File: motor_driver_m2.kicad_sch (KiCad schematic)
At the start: 32 parts, among them J7 Conn_01x01_Pin, J8 Conn_01x01_Pin, J9 Conn_01x01_Pin, M2 DRV8320SRTVR, Q10 NP80N06D6, Q11 NP80N06D6, Q12 NP80N06D6, Q7 NP80N06D6, Q8 NP80N06D6, Q9 NP80N06D6

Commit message: ...
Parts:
- C28: renamed from C25; footprint easyeda2kicad:C0603 -> easyeda2kicad:C0402
- renumbered C24 to C27, C26 to C29, C27 to C30, C28 to C31, C29 to C32, C30 to C33, C31 to C34, J8 to J7, J9 to J8, J7 to J9, R23 to R21, R27 to R22, R28 to R23, R29 to R24, R30 to R25, R31 to R26, R32 to R27, R33 to R28, R34 to R29, R35 to R30, R36 to R31, R37 to R32, R38 to R33, R39 to R34
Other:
- moved on the sheet: J7, J8, J9

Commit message: ...
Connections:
- net SCLK: no longer names the net of M2.20 (SCLK)
- net SDI: no longer names the net of M2.19 (SDI)
- net SDO: no longer names the net of M2.18 (SDO)
- no-connect marks 0 -> 3
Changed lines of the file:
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@@
 		(color 0 0 0 0)
 	)
+	(no_connect
+		(at 92.71 80.01)
+	)
+	(no_connect
+		(at 92.71 77.47)
+	)
+	(no_connect
+		(at 92.71 74.93)
+	)
 	(wire
 		(pts
@@
 	(wire
 		(pts
-			(xy 105.41 74.93) (xy 92.71 74.93)
-		)
-		(stroke
-			(width 0)
-			(type default)
-		)
-	)
-	(wire
-		(pts
 			(xy 105.41 57.15) (xy 92.71 57.15)
 		)
@@
 	(wire
 		(pts
-			(xy 105.41 77.47) (xy 92.71 77.47)
-		)
-		(stroke
-			(width 0)
-			(type default)
-		)
-	)
-	(wire
-		(pts
 			(xy 77.47 161.29) (xy 77.47 162.56)
 		)
@@
 	(wire
 		(pts
-			(xy 92.71 80.01) (xy 105.41 80.01)
-		)
-		(stroke
-			(width 0)
-			(type default)
-		)
-	)
-	(wire
-		(pts
 			(xy 21.59 50.8) (xy 21.59 49.53)
 		)
@@
 		)
 	)
-	(global_label "SCLK"
-		(shape input)
-		(at 105.41 74.93 0)
-		(fields_autoplaced yes)
-		(effects
-			(font
-				(size 1.27 1.27)
-			)
-			(justify left)
-		)
-		(property "Intersheetrefs" "${INTERSHEET_REFS}"
-			(at 113.1728 74.93 0)
-			(effects
-				(font
-					(size 1.27 1.27)
-				)
-				(justify left)
-				(hide yes)
-			)
-		)
-	)
 	(global_label "B+"
 		(shape input)
@@
 		)
 	)
-	(global_label "SDO"
-		(shape input)
-		(at 105.41 80.01 0)
-		(fields_autoplaced yes)
-		(effects
-			(font
-				(size 1.27 1.27)
-			)
-			(justify left)
-		)
-		(property "Intersheetrefs" "${INTERSHEET_REFS}"
-			(at 112.2052 80.01 0)
-			(effects
-				(font
-					(size 1.27 1.27)
-				)
-				(justify left)
-				(hide yes)
-			)
-		)
-	)
 	(global_label "GLB2"
 		(shape input)
@@
 			(effects
 				(font
-					(size 1.27 1.27)
-				)
-				(justify left)
-				(hide yes)
-			)
-		)
-	)
-	(global_label "SDI"
-		(shape input)
-		(at 105.41 77.47 0)
-		(fields_autoplaced yes)
-		(effects
-			(font
-				(size 1.27 1.27)
-			)
-			(justify left)
-		)
-		(property "Intersheetrefs" "${INTERSHEET_REFS}"
-			(at 111.4795 77.47 0)
-			(effects
-				(font

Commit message: ...
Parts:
- added C52: 100nF, easyeda2kicad:C0603, symbol Device:C
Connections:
- net B+: now also C52.1
- net GND: now also C52.2
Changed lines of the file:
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@@
 	(generator_version "9.0")
 	(paper "A4")
+	(text_box "BEMF\n"
+		(exclude_from_sim no)
+		(at 29.21 130.81 0)
+		(size 119.38 43.18)
+		(margins 0.9525 0.9525 0.9525 0.9525)
+		(stroke
+			(width 0)
+			(type solid)
+		)
+		(fill
+			(type none)
+		)
+		(effects
+			(font
+				(size 1.27 1.27)
+			)
+			(justify left top)
+		)
+	)
 	(junction
 		(at 222.25 125.73)
@@
 	(wire
 		(pts
+			(xy 90.17 115.57) (xy 90.17 111.76)
+		)
+		(stroke
+			(width 0)
+			(type default)
+		)
+	)
+	(wire
+		(pts
 			(xy 39.37 152.4) (xy 39.37 153.67)
 		)
@@
 	(wire
 		(pts
+			(xy 90.17 100.33) (xy 90.17 104.14)
+		)
+		(stroke
+			(width 0)
+			(type default)
+		)
+	)
+	(wire
+		(pts
 			(xy 45.72 161.29) (xy 45.72 162.56)
 		)
@@
 		)
 	)
+	(global_label "B+"
+		(shape input)
+		(at 90.17 100.33 180)
+		(fields_autoplaced yes)
+		(effects
+			(font
+				(size 1.27 1.27)
+			)
+			(justify right)
+		)
+		(property "Intersheetrefs" "${INTERSHEET_REFS}"
+			(at 84.3424 100.33 0)
+			(effects
+				(font
+					(size 1.27 1.27)
+				)
+				(justify right)
+				(hide yes)
+			)
+		)
+	)
 	(global_label "INHC_M2"
 		(shape input)
@@
 	(symbol
 		(lib_id "power:GND")
+		(at 90.17 115.57 0)
+		(unit 1)
+		(exclude_from_sim no)
+		(in_bom yes)
+		(on_board yes)
+		(dnp no)
+		(property "Reference" "#PWR0123"
+			(at 90.17 121.92 0)
+			(effects
+				(font
+					(size 1.27 1.27)
+				)
+				(hide yes)
+			)
+		)
+		(property "Value" "GND"
+			(at 92.202 120.396 0)
+			(effects
+				(font
+					(size 1.27 1.27)
+				)
+				(justify right)
+			)
+		)
+		(property "Footprint" ""
+			(at 90.17 115.57 0)
+			(effects
+				(font
+					(size 1.27 1.27)
+				)
+				(hide yes)
+			)
+		)
+		(property "Datasheet" ""
+			(at 90.17 115.57 0)
+			(effects
+				(font
+					(size 1.27 1.27)
+				)
+				(hide yes)
+			)
+		)
+		(property "Description" "Power symbol creates a global label with name \"GND\" , ground"
+			(at 90.17 115.57 0)
+			(effects
+				(font
+					(size 1.27 1.27)
+				)
+				(hide yes)
+			)
+		)
+		(pin "1"
+		)
+		(instances
+			(project "esc"
+				(path "/131092d7-5dad-4272-a758-a2445b6ec99c/e38f1183-feeb-4e2e-a0f6-2b964e24b911"
+					(reference "#PWR0123")
+					(unit 1)
+				)
+			)
+		)
+	)
+	(symbol
+		(lib_id "power:GND")
 		(at 231.14 57.15 270)
 		(unit 1)
@@
 					(unit 1)
 				)
+			)
+		)
+	)
+	(symbol
+		(lib_id "Device:C")
+		(at 90.17 107.95 0)
+		(unit 1)
+		(exclude_from_sim no)
+		(in_bom yes)
+		(on_board yes)
+		(dnp no)
+		(property "Reference" "C52"
+			(at 92.964 107.188 0)
+			(effects
+				(font
+					(size 1.27 1.27)
+				)
+				(justify left)
+			)
+		)
+		(property "Value" "100nF"
+			(at 92.964 108.966 0)
+			(effects
+				(font
+					(size 1.27 1.27)
+				)
+				(justify left)
+			)
+		)
+		(property "Footprint" "easyeda2kicad:C0603"
+			(at 91.1352 111.76 0)
+			(effects
+				(font
+					(size 1.27 1.27)
+				)
+				(hide yes)
+			)
+		)
+		(property "Datasheet" "~"
+			(at 90.17 107.95 0)
+			(effects
+				(font
+					(size 1.27 1.27)
+				)
+				(hide yes)
+			)
+		)
+		(property "Description" "Unpolarized capacitor"
+			(at 90.17 107.95 0)
+			(effects
+				(font
+					(size 1.27 1.27)
+				)
+				(hide yes)
+			)
+		)
+		(pin "1"
+		)
+		(pin "2"
+		)
+		(instances
+			(project "esc"
+				(path "/131092d7-5dad-4272-a758-a2445b6ec99c/e38f1183-feeb-4e2e-a0f6-2b964e24b911"
+					(reference "C52")
+					(unit 1)
+				)

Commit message: complete change in architecture,work in progress
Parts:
- removed M2: DRV8320SRTVR, easyeda2kicad:WQFN-32_L5.0-W5.0-P0.50-TL-EP3.5, symbol easyeda2kicad:DRV8320SRTVR
- added C22, C64, C65: 100nF, easyeda2kicad:C0603, symbol Device:C
- added C23: 100nF, easyeda2kicad:C0402, symbol Device:C
- added C43, C44: 1uF, easyeda2kicad:C0402, symbol Device:C
- added J18: Conn_01x01_Pin, deshan:Conn_1x1_small, symbol Connector:Conn_01x01_Pin
- added R66, R67, R68: 10k, easyeda2kicad:R0402, symbol Device:R
- added R69: 50k, easyeda2kicad:R0402, symbol Device:R
- added U6: STDRIVE101, easyeda2kicad:QFN-24_L4.0-W4.0-P0.50-BL-EP2.7, symbol easyeda2kicad:STDRIVE101
- added U7: STM32C011F6U6TR, easyeda2kicad:UFQFPN-20_L3.0-W3.0-P0.50-TL, symbol easyeda2kicad:STM32C011F6U6TR
- C27: value >10uF -> 100nF; footprint easyeda2kicad:C0603 -> easyeda2kicad:C0402
- C28: value 0.1uF -> 4.7uF; footprint easyeda2kicad:C0402 -> easyeda2kicad:C0603
- C29: value 1uF -> 100nF; footprint easyeda2kicad:C0603 -> easyeda2kicad:C0402
- C30: value 47nF -> 4.7uF; footprint easyeda2kicad:C0603 -> easyeda2kicad:C0402
- C31: footprint easyeda2kicad:C0603 -> easyeda2kicad:C0402
- R21: value 10k -> 18k
- R22: value 10k -> 39k
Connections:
- net 3V3: now also C27.1, C30.1, R66.2, U7.2 (VDD/VDDA)
- net B+: now also C23.1, C64.1, C65.1, U6.4 (VS); no longer C27.1, C28.1, C29.1
- net GND: now also C29.2, C30.2, C22.2, C23.2, C64.2, C65.2, R67.2, R68.1, R69.2, U6.25 (EP), U7.3 (VSS/VSSA); no longer C31.2, R24.2, R26.2, R28.2
- net at R22.1: now also U6.6 (nFAULT)
- net OUT1: now reaches C31.1
- net OUT1: now also J7.1 (Pin_1), Q7.1 (S), Q7.2 (S), Q7.3 (S), Q8.5 (D), Q8.6 (D), Q8.7 (D), Q8.8 (D), Q8.9 (D), R29.2, U6.23 (OUT1)
- net GHA2: no longer names the net of Q7.4 (G), R23.1
- net GHB2: no longer names the net of Q9.4 (G), R25.1
- net GHC2: no longer names the net of Q11.4 (G), R27.1
- net GLA2: no longer names the net of Q8.4 (G), R24.1
- net GLB2: no longer names the net of Q10.4 (G), R26.1
- net GLC2: no longer names the net of Q12.4 (G), R28.1
- net PUPL2: no longer names the net of R21.2
- net PUPL2: now also R67.1, U6.3 (SCREF)
- removed net SHA2: J7.1 (Pin_1), Q7.1 (S), Q7.2 (S), Q7.3 (S), Q8.5 (D), Q8.6 (D), Q8.7 (D), Q8.8 (D), Q8.9 (D), R23.2, R29.2
- net SHB2 renamed OUT2
- net OUT2: now also C43.1, U6.19 (OUT2); no longer R25.2
- net SHC2 renamed OUT3
- net OUT3: now also C44.1, U6.15 (OUT3); no longer R27.2
- new net: C31.2, U6.21 (BOOT1)
- new net: R68.2, U6.1 (CP)
- new net: C29.1, R66.1, U7.4 (PF2-NRST)
- new net: C43.2, U6.17 (BOOT2)
- new net: C22.1, C28.1, U6.5 (REG12)
- new net: C44.2, U6.13 (BOOT3)
- new net: R69.1, U6.2 (DT/MODE)
- new net DShot_M2: J18.1 (Pin_1)
- new net EN1_M2: U6.10 (INL1/EN1), U7.12 (PA7)
- new net EN2_M2: U6.11 (INL2/EN2), U7.11 (PA6)
- new net EN3_M2: U6.12 (INL3/EN3), U7.10 (PA5)
- new net GHS1: R23.2, U6.22 (GHS1)
- new net GHS2: R25.2, U6.18 (GHS2)
- new net GHS3: R27.2, U6.14 (GHS3)
- new net GLS1: R24.2, U6.24 (GLS1)
- new net GLS2: R26.2, U6.20 (GLS2)
- new net GLS3: R28.2, U6.16 (GLS3)
- new net INH1_M2: U6.7 (INH1/IN1), U7.15 (PA12[PA10])
- new net INH2_M2: U6.8 (INH2/IN2), U7.14 (PA11[PA9])
- new net INH3_M2: U6.9 (INH3/IN3), U7.13 (PA8)
- new net SWCLK: U7.17 (PA14-BOOT0)
- new net SWDIO_M2: U7.16 (PA13)
- no-connect marks 3 -> 2
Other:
- moved on the sheet: C32, C33, C34, C52, J7, J8, J9, R23, R24, R25, R26, R27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

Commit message: ...
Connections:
- net DShot_M2: now also U7.6 (PA1)
- net PHASE_A_M1: now also U7.8 (PA3)
- net PHASE_B_M1: now also U7.7 (PA2)
- net PHASE_C_M1: now also U7.9 (PA4)
- net SWCLK renamed SWCLK_L
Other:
- title: (none) -> MOTOR DRIVER M2
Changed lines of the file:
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@@
 	(generator_version "10.0")
 	(paper "A4")
+	(title_block
+		(title "MOTOR DRIVER M2")
+		(rev "1.0")
+	)
 	(text_box "BEMF\n"
 		(exclude_from_sim no)
@@
 	(global_label "PHASE_A_M1"
 		(shape input)
-		(at 135.89 27.94 180)
+		(at 59.69 58.42 180)
 		(fields_autoplaced yes)
 		(effects
@@
 		)
 		(property "Intersheetrefs" "${INTERSHEET_REFS}"
-			(at 121.1725 27.94 0)
+			(at 44.9725 58.42 0)
 			(hide yes)
 			(show_name no)
@@
 	(global_label "PHASE_B_M1"
 		(shape input)
-		(at 135.89 25.4 180)
+		(at 59.69 55.88 180)
 		(fields_autoplaced yes)
 		(effects
@@
 		)
 		(property "Intersheetrefs" "${INTERSHEET_REFS}"
-			(at 120.9911 25.4 0)
+			(at 44.7911 55.88 0)
 			(hide yes)
 			(show_name no)
@@
 		)
 	)
-	(global_label "SWCLK"
+	(global_label "SWCLK_L"
 		(shape input)
 		(at 113.03 48.26 0)
@@
 		)
 		(property "Intersheetrefs" "${INTERSHEET_REFS}"
-			(at 122.2442 48.26 0)
+			(at 124.2399 48.26 0)
 			(hide yes)
 			(show_name no)
@@
 		)
 	)
+	(global_label "DShot_M2"
+		(shape input)
+		(at 59.69 53.34 180)
+		(fields_autoplaced yes)
+		(effects
+			(font
+				(size 1.27 1.27)
+			)
+			(justify right)
+		)
+		(property "Intersheetrefs" "${INTERSHEET_REFS}"
+			(at 47.5731 53.34 0)
+			(hide yes)
+			(show_name no)
+			(do_not_autoplace no)
+			(effects
+				(font
+					(size 1.27 1.27)
+				)
+				(justify right)
+			)
+		)
+	)
 	(global_label "B+"
 		(shape input)
@@
 	(global_label "PHASE_C_M1"
 		(shape input)
-		(at 135.89 30.48 180)
+		(at 59.69 60.96 180)
 		(fields_autoplaced yes)
 		(effects
@@
 		)
 		(property "Intersheetrefs" "${INTERSHEET_REFS}"
-			(at 120.9911 30.48 0)
+			(at 44.7911 60.96 0)
 			(hide yes)
 			(show_name no)

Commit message: ...
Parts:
- J18: footprint deshan:Conn_1x1_small -> deshan:Conn_01x01_Pin
- J7, J8, J9: footprint deshan:Conn_1x1 -> deshan:Conn_01x01_Power
- renumbered C29 to C16, C27 to C17, C30 to C18, C23 to C19, C22 to C20, C28 to C21, C31 to C22, C43 to C23, C44 to C24, C52 to C25, C64 to C26, C65 to C27, C32 to C28, C33 to C29, C34 to C30, R66 to R19, R21 to R20, R67 to R21, R68 to R22, R69 to R23, R22 to R24, R23 to R25, R24 to R26, R25 to R27, R26 to R28, R27 to R29, R28 to R30, R29 to R31, R30 to R32, R31 to R33, R32 to R34, R33 to R35, R34 to R36
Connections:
- net PHASE_A_M1 is gone; now on net PHASE_B_M2: U7.8 (PA3)
- net PHASE_B_M1 is gone; now on net PHASE_C_M2: U7.7 (PA2)
- net PHASE_C_M1 is gone; now on net PHASE_A_M2: U7.9 (PA4)
- net SWCLK_L renamed SWCLK_M2

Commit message: ...
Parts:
- renumbered J18 to DShot_M2, U6 to GD2, J7 to J4, J8 to J5, J9 to J6, U7 to M2
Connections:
- no-connect marks 2 -> 5
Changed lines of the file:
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@@
 	)
 	(no_connect
+		(at 113.03 45.72)
+	)
+	(no_connect
 		(at 113.03 40.64)
 	)
 	(no_connect
+		(at 113.03 43.18)
+	)
+	(no_connect
+		(at 59.69 50.8)
+	)
+	(no_connect
 		(at 59.69 40.64)
 	)
@@
 		(dnp no)
 		(fields_autoplaced yes)
-		(property "Reference" "J18"
+		(property "Reference" "DShot_M2"
 			(at 165.1 125.0949 90)
 			(show_name no)
@@
 			(project "esc"
 				(path "/131092d7-5dad-4272-a758-a2445b6ec99c/e38f1183-feeb-4e2e-a0f6-2b964e24b911"
-					(reference "J18")
+					(reference "DShot_M2")
 					(unit 1)
 				)
@@
 		(dnp no)
 		(fields_autoplaced yes)
-		(property "Reference" "U7"
+		(property "Reference" "M2"
 			(at 86.36 33.02 0)
 			(show_name no)
@@
 			(project "esc"
 				(path "/131092d7-5dad-4272-a758-a2445b6ec99c/e38f1183-feeb-4e2e-a0f6-2b964e24b911"
-					(reference "U7")
+					(reference "M2")
 					(unit 1)
 				)
@@
 		(dnp no)
 		(fields_autoplaced yes)
-		(property "Reference" "J7"
+		(property "Reference" "J4"
 			(at 151.765 161.29 0)
 			(show_name no)
@@
 			(project "esc"
 				(path "/131092d7-5dad-4272-a758-a2445b6ec99c/e38f1183-feeb-4e2e-a0f6-2b964e24b911"
-					(reference "J7")
+					(reference "J4")
 					(unit 1)
 				)
@@
 		(dnp no)
 		(fields_autoplaced yes)
-		(property "Reference" "U6"
+		(property "Reference" "GD2"
 			(at 76.2 91.44 0)
 			(show_name no)
@@
 			(project "esc"
 				(path "/131092d7-5dad-4272-a758-a2445b6ec99c/e38f1183-feeb-4e2e-a0f6-2b964e24b911"
-					(reference "U6")
+					(reference "GD2")
 					(unit 1)
 				)
@@
 		(dnp no)
 		(fields_autoplaced yes)
-		(property "Reference" "J8"
+		(property "Reference" "J5"
 			(at 151.765 170.18 0)
 			(show_name no)
@@
 			(project "esc"
 				(path "/131092d7-5dad-4272-a758-a2445b6ec99c/e38f1183-feeb-4e2e-a0f6-2b964e24b911"
-					(reference "J8")
+					(reference "J5")
 					(unit 1)
 				)
@@
 		(dnp no)
 		(fields_autoplaced yes)
-		(property "Reference" "J9"
+		(property "Reference" "J6"
 			(at 151.765 181.61 0)
 			(show_name no)
@@
 			(project "esc"
 				(path "/131092d7-5dad-4272-a758-a2445b6ec99c/e38f1183-feeb-4e2e-a0f6-2b964e24b911"
-					(reference "J9")
+					(reference "J6")
 					(unit 1)
 				)

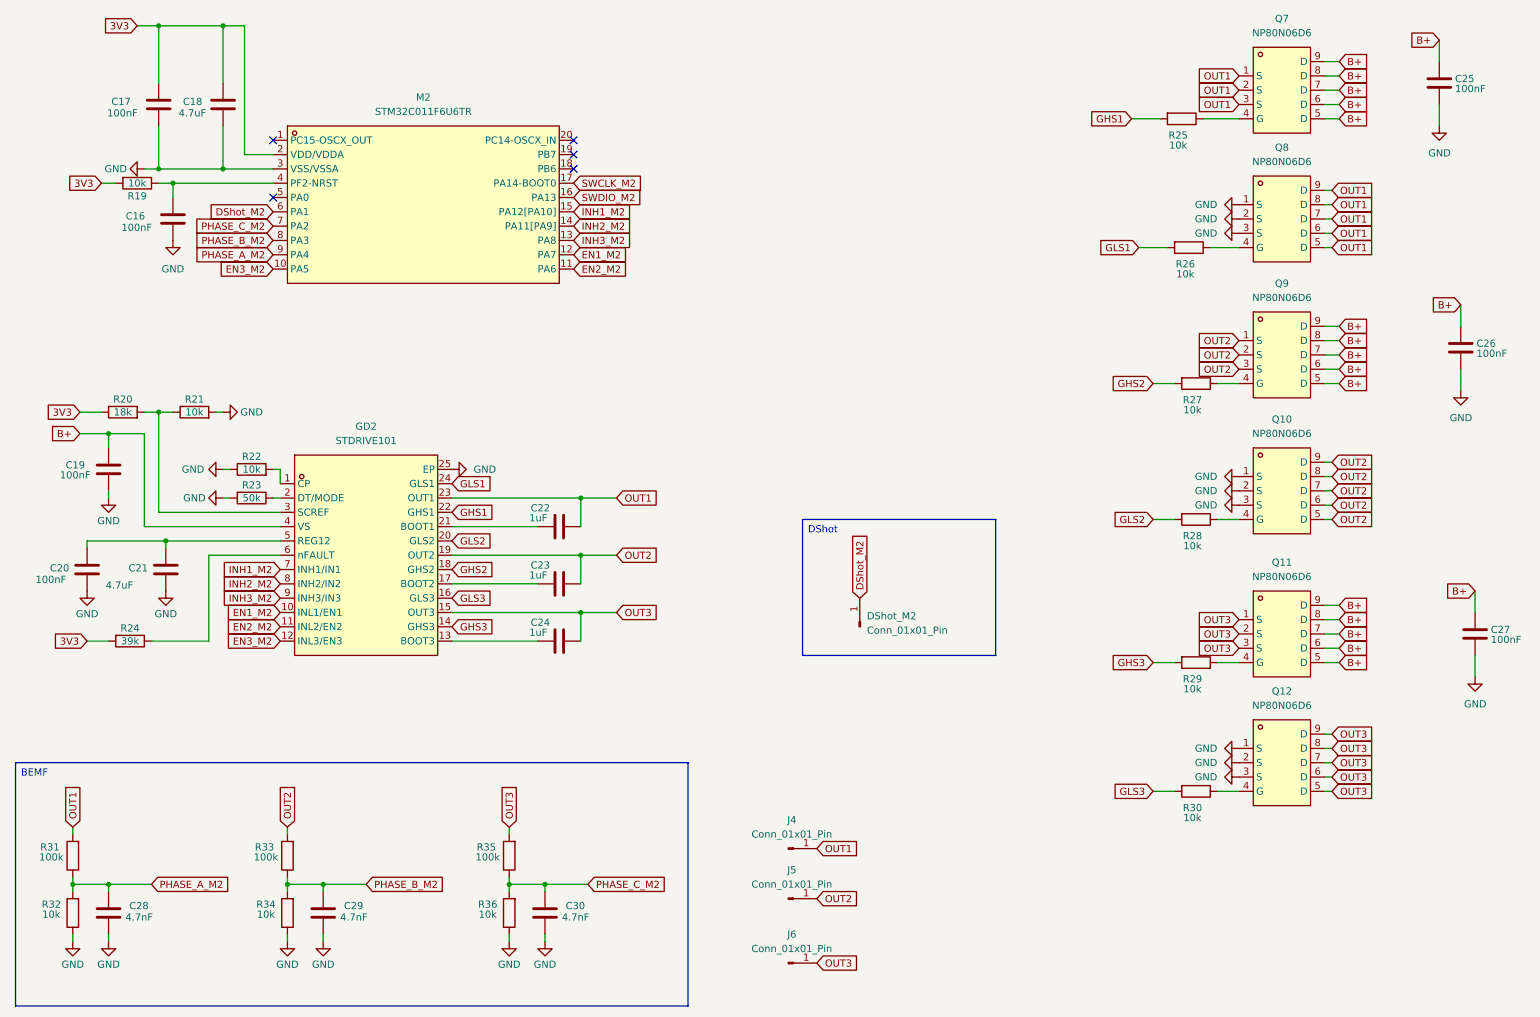
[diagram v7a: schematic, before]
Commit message: change in architecture with horizonatal half bridge
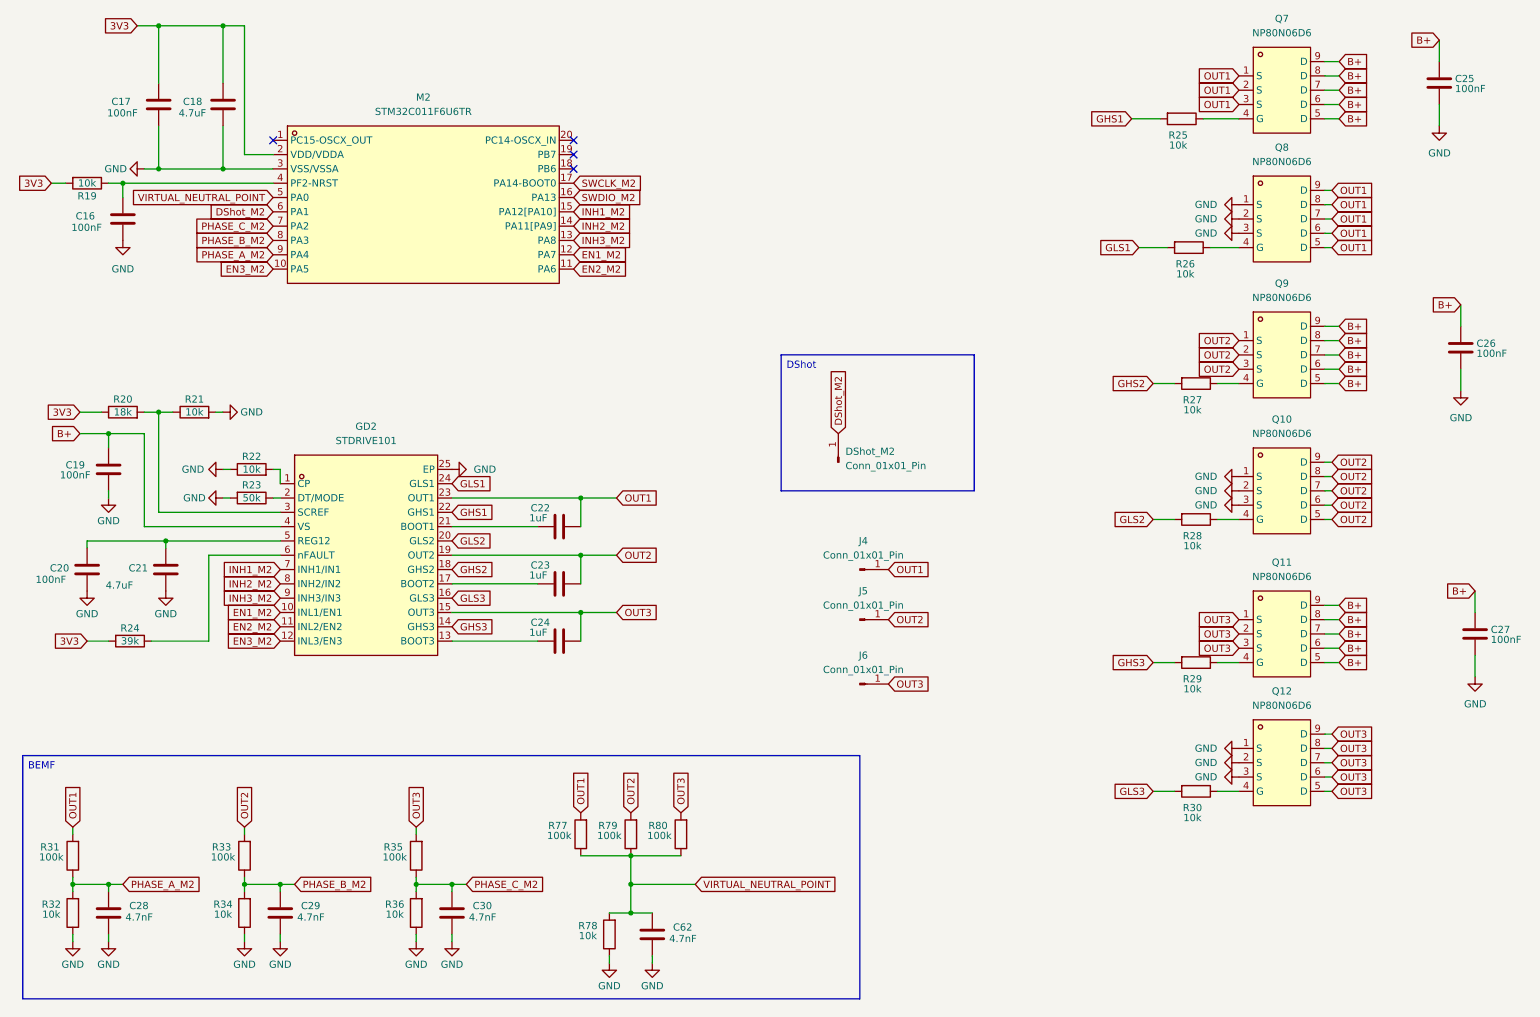
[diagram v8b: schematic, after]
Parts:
- added C62: 4.7nF, easyeda2kicad:C0402, symbol Device:C
- added R77, R79, R80: 100k, easyeda2kicad:R0402, symbol Device:R
- added R78: 10k, easyeda2kicad:R0402, symbol Device:R
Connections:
- net GND: now also C62.2, R78.1
- net OUT1: now also R77.2
- net OUT2: now also R79.2
- net OUT3: now also R80.2
- net VIRTUAL_NEUTRAL_POINT: now reaches M2.5 (PA0)
- net VIRTUAL_NEUTRAL_POINT: now also C62.1, R77.1, R78.2, R79.1, R80.1
- no-connect marks 5 -> 4
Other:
- moved on the sheet: C16, C29, C30, DShot_M2, J4, J5, J6, R19, R33, R34, R35, R36
